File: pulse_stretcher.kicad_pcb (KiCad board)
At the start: 2 copper layers, 71 x 64 mm, 77 parts, among them J1 5VDC, J2 SMA, J3 SMA, U1 MAX1735, U2 MCP1824ST-33, U3 MCP1824ST-25, U4 MC100LVEL31, U5 SY100ELT21L, U6 74LVC1G04, U7 AUC2G04, U8 AUC2G04, U9 AUC2G04

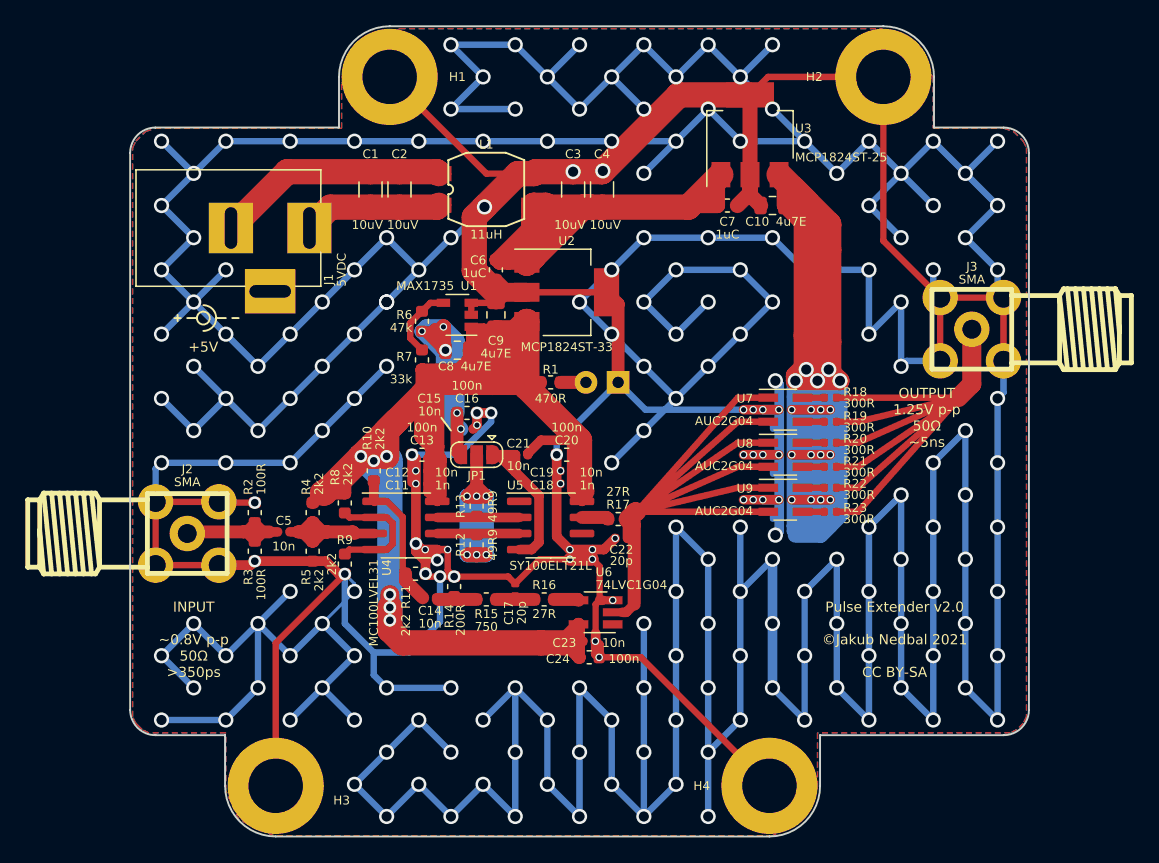
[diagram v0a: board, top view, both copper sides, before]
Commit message: Added ~clock_enable
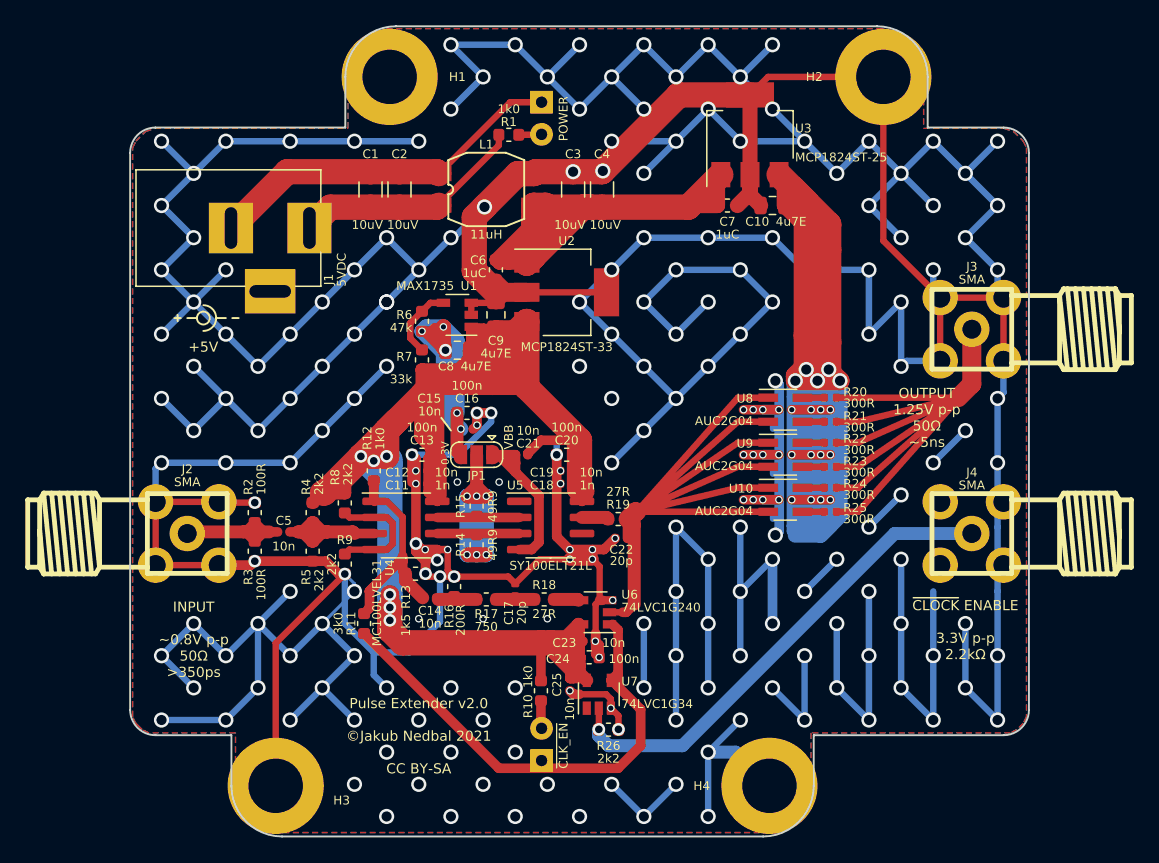
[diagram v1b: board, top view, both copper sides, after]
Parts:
- added C25: 10n, Capacitor_SMD:C_0402_1005Metric, F.Cu at (126.2, 98.8)
- added D2: orange, LED_THT:LED_D3.0mm, B.Cu at (124.0, 104.8)
- added J4: SMA, jakub:SMA_5.0mm, F.Cu at (158.0, 86.9)
- added R10: 1k0, Resistor_SMD:R_0603_1608Metric, F.Cu at (124.0, 99.3)
- added R11: 3k0, Resistor_SMD:R_0603_1608Metric, F.Cu at (110.0, 94.0)
- added R26: 2k2, Resistor_SMD:R_0603_1608Metric, F.Cu at (129.3, 102.4)
- added U7: 74LVC1G34, Package_TO_SOT_SMD:SOT-23-5, F.Cu at (128.5, 99.6)
- D1: value orange -> green
- R1: value 470R -> 1k0
- R12: renamed from R10; value 2k2 -> 1k0
- R13: renamed from R11; value 2k2 -> 1k5
- U6: value 74LVC1G04 -> 74LVC1G240; footprint Package_TO_SOT_SMD:SOT-23-5_HandSoldering -> Package_TO_SOT_SMD:SOT-23-5
- moved D1 22.9 mm to (124.0, 52.8), turned to 270 degrees
- moved R1 19.8 mm to (121.4, 55.4)
- renumbered C27 to C26, C28 to C27, C29 to C28, C30 to C29, C31 to C30, C32 to C31, C33 to C32, C34 to C33, C35 to C34, C25 to C35, C26 to C36, R12 to R14, R13 to R15, R14 to R16, R15 to R17, R16 to R18, R17 to R19, R18 to R20, R19 to R21, R20 to R22, R21 to R23, R22 to R24, R23 to R25, U9 to U10, U7 to U8, U8 to U9
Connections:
- net Net-(C14-Pad2) renamed /SET
- D1 pad 1: GND -> Net-(C1-Pad2)
- R1 pad 1: +3V3 -> Net-(C1-Pad1)
- U6 pad 1: (no net) -> /~ENABLEBUF
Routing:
- net GND: track 1075.7 -> 856.5 mm, vias 227 -> 223
- net /~ENABLEBUF: track 0.00 -> 39.9 mm
- net /~ENABLE: track 0.00 -> 38.9 mm, vias 0 -> 1
- net +3V3: track 165.8 -> 178.4 mm
- net Net-(C1-Pad2): track 18.3 -> 28.8 mm
- net /SET: track 12.0 -> 19.6 mm
- net Net-(C1-Pad1): track 11.0 -> 18.5 mm
- net Net-(D2-Pad2): track 0.00 -> 2.20 mm
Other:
- outline, holes or cut-outs redrawn
- board text added: "0.3V"
- board text added: "POWER"
- board text added: "VBB"
- board text added: "~CLK_EN"
- board text added: "~CLOCK ENABLE 3.3V p-p 2.2kΩ"

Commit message: Added comment about RC filter being optional
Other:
- board text added: "Optional 0Ω R19 to bypass"

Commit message: Production run
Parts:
- C17, C22: footprint Capacitor_SMD:C_0402_1005Metric -> Capacitor_SMD:C_0603_1608Metric
- R17: value 750 -> 750R
- moved C22 0.92 mm to (130.0, 88.1)
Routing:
- net /OUTPUT: track 84.6 -> 85.5 mm
- net GND: track 856.5 -> 855.6 mm
